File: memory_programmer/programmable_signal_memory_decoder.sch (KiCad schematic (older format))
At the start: 5 parts

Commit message: ram pcb
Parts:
- U3: renamed from U?; footprint (none) -> Package_DIP:DIP-16_W7.62mm_LongPads
- U4, U5, U6, U7: renamed from U?; footprint (none) -> Package_DIP:DIP-20_W7.62mm_LongPads
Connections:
- net D0: no longer U4.3 (D0), U5.3 (D0), U6.3 (D0)
- net D1: no longer U4.4 (D1), U5.4 (D1), U6.4 (D1), U7.4 (D1)
- net D2: no longer U4.7 (D2), U5.7 (D2), U6.7 (D2), U7.7 (D2)
- net D3: no longer U4.8 (D3), U5.8 (D3), U6.8 (D3), U7.8 (D3)
- net D4: no longer U4.13 (D4), U5.13 (D4), U6.13 (D4), U7.13 (D4)
- net D5: no longer U4.14 (D5), U5.14 (D5), U6.14 (D5), U7.14 (D5)
- net D6: no longer U4.17 (D6), U5.17 (D6), U6.17 (D6), U7.17 (D6)
- net D7: no longer U4.18 (D7), U5.18 (D7), U6.18 (D7), U7.18 (D7)
- net P0: now reaches U7.3 (D0)
- net P0: now also U4.3 (D0), U5.3 (D0), U6.3 (D0)
- net A0 renamed AD0
- net A1 renamed AD1
- net A10 renamed AD10
- net A11 renamed AD11
- net A12 renamed AD12
- net A13 renamed AD13
- net A14 renamed AD14
- net A15 renamed AD15
- net A2 renamed AD2
- net A3 renamed AD3
- net A4 renamed AD4
- net A5 renamed AD5
- net A6 renamed AD6
- net A7 renamed AD7
- net A8 renamed AD8
- net A9 renamed AD9
- new net P1: U4.4 (D1), U5.4 (D1), U6.4 (D1), U7.4 (D1)
- new net P2: U4.7 (D2), U5.7 (D2), U6.7 (D2), U7.7 (D2)
- new net P3: U4.8 (D3), U5.8 (D3), U6.8 (D3), U7.8 (D3)
- new net P4: U4.13 (D4), U5.13 (D4), U6.13 (D4), U7.13 (D4)
- new net P5: U4.14 (D5), U5.14 (D5), U6.14 (D5), U7.14 (D5)
- new net P6: U4.17 (D6), U5.17 (D6), U6.17 (D6), U7.17 (D6)
- new net P7: U4.18 (D7), U5.18 (D7), U6.18 (D7), U7.18 (D7)

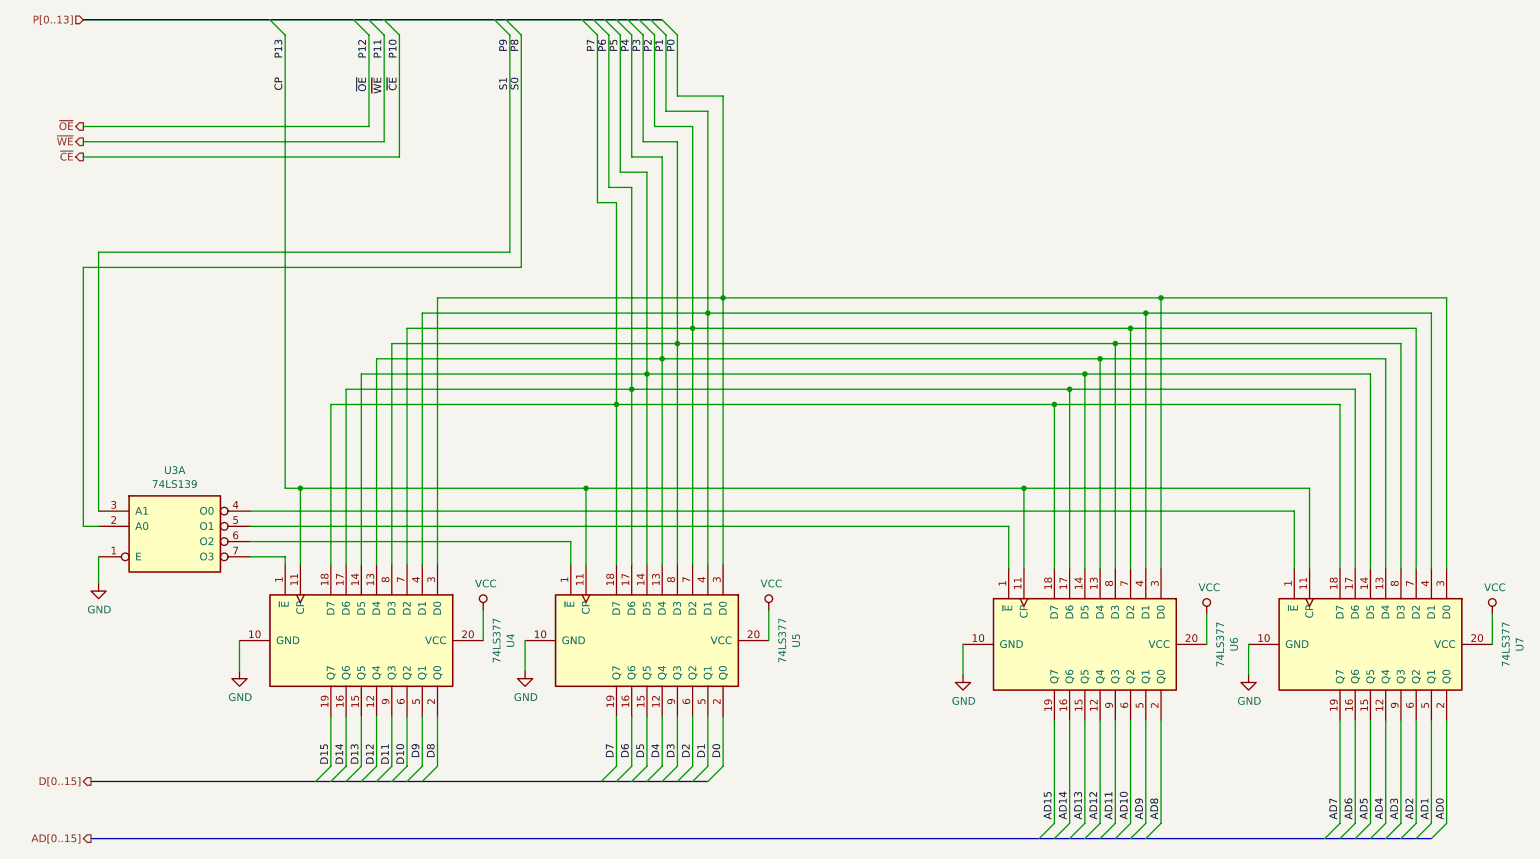
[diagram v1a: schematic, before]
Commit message: memory programmer and cu
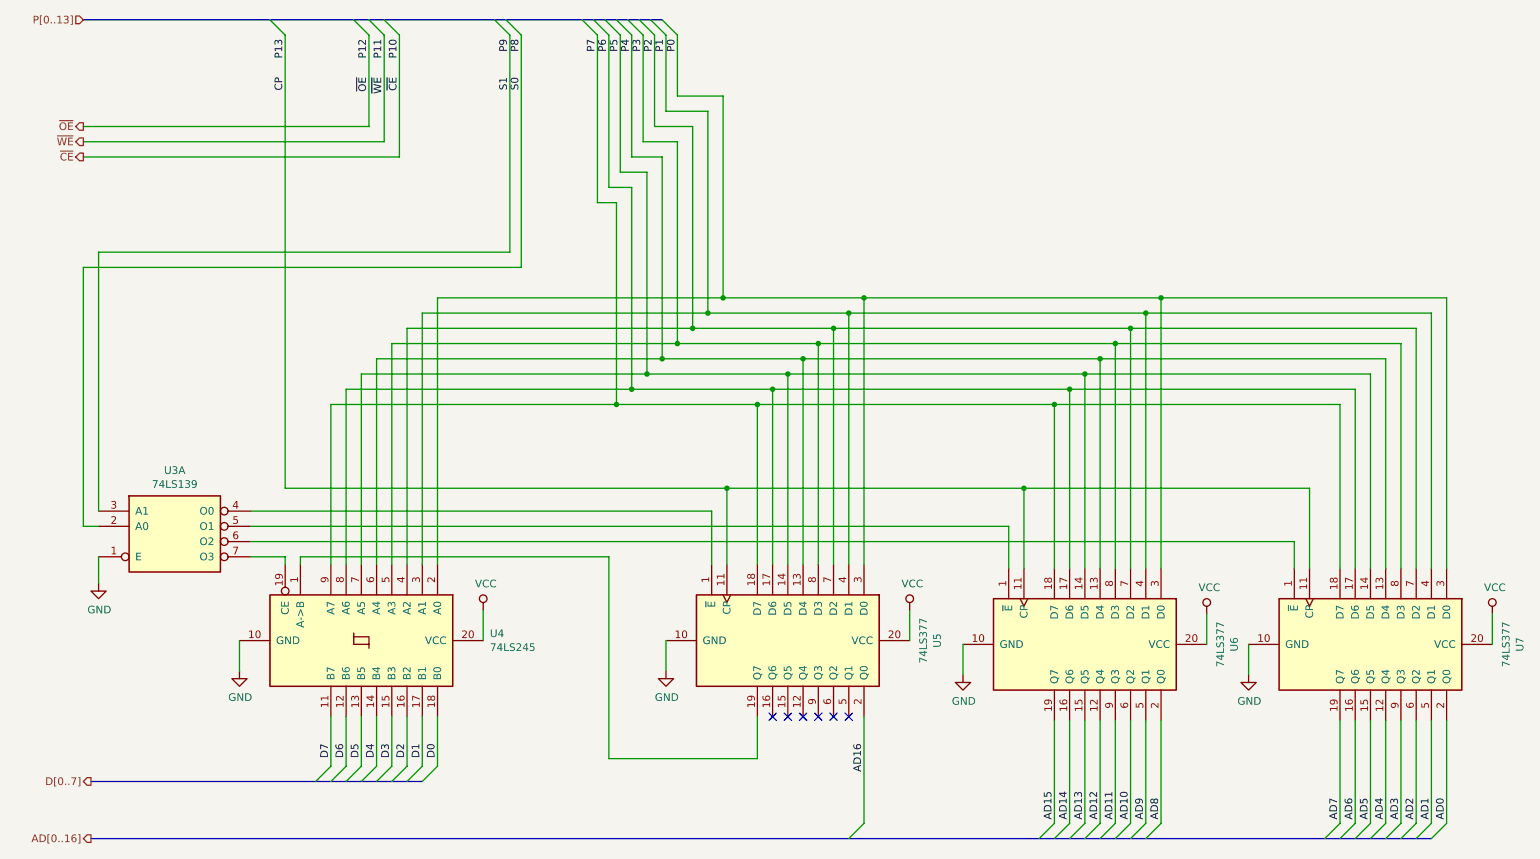
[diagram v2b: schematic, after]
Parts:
- removed U4: 74LS377, Package_DIP:DIP-20_W7.62mm_LongPads, symbol 74xx:74LS377
- added U4: 74LS245, Package_DIP:DIP-20_W7.62mm_LongPads, symbol 74xx:74LS245
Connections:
- net D0: now also U4.18 (B0); no longer U5.2 (Q0)
- net D1: now also U4.17 (B1); no longer U5.5 (Q1)
- net D2: now also U4.16 (B2); no longer U5.6 (Q2)
- net D3: now also U4.15 (B3); no longer U5.9 (Q3)
- net D4: now also U4.14 (B4); no longer U5.12 (Q4)
- net D5: now also U4.13 (B5); no longer U5.15 (Q5)
- net D6: now also U4.12 (B6); no longer U5.16 (Q6)
- net D7: now also U4.11 (B7); no longer U5.19 (Q7)
- net GND: now also U4.10 (GND)
- net P0: now also U4.2 (A0)
- net P1: now also U4.3 (A1)
- net P2: now also U4.4 (A2)
- net P3: now also U4.5 (A3)
- net P4: now also U4.6 (A4)
- net P5: now also U4.7 (A5)
- net P6: now also U4.8 (A6)
- net P7: now also U4.9 (A7)
- net VCC: now also U4.20 (VCC)
- net at U7.1 (~E): now also U3.6 (O2); no longer U3.4 (O0)
- net at U5.1 (~E): now also U3.4 (O0); no longer U3.6 (O2)
- net at U3.7 (O3): now also U4.19 (CE)
- new net: U4.1 (A->B), U5.19 (Q7)
- new net AD16: U5.2 (Q0)
- no-connect marks 0 -> 6
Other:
- moved on the sheet: U5
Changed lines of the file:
@@
 $Descr A4 11693 8268
 encoding utf-8
-Sheet 5 5
+Sheet 3 3
 Title ""
 Date ""
@@
 L 74xx:74LS377 U?
 U 1 1 5D3D9F68
-P 4725 5050
+P 5650 5050
 AR Path="/5D3716A7/5D3D9F68" Ref="U?"  Part="1"
 AR Path="/5D371796/5D3D9F68" Ref="U?"  Part="1"
@@
 AR Path="/5D35D52D/5D3B2113/5D3D9F68" Ref="U?"  Part="1"
 AR Path="/5EDF08FE/5D3D9F68" Ref="U5"  Part="1"
-F 0 "U5" H 4725 6031 50  0000 C CNN
-F 1 "74LS377" H 4725 5940 50  0000 C CNN
-F 2 "Package_DIP:DIP-20_W7.62mm_LongPads" H 4725 5050 50  0001 C CNN
-F 3 "http://www.ti.com/lit/gpn/sn74LS377" H 4725 5050 50  0001 C CNN
-	1    4725 5050
+F 0 "U5" H 5650 6031 50  0000 C CNN
+F 1 "74LS377" H 5650 5940 50  0000 C CNN
+F 2 "Package_DIP:DIP-20_W7.62mm_LongPads" H 5650 5050 50  0001 C CNN
+F 3 "http://www.ti.com/lit/gpn/sn74LS377" H 5650 5050 50  0001 C CNN
+	1    5650 5050
 	0    1    1    0
 $EndComp
@@
 L power:GND #PWR014
 U 1 1 5D3D9F6E
-P 3925 5250
-F 0 "#PWR014" H 3925 5000 50  0001 C CNN
-F 1 "GND" H 3930 5077 50  0000 C CNN
-F 2 "" H 3925 5250 50  0001 C CNN
-F 3 "" H 3925 5250 50  0001 C CNN
-	1    3925 5250
-	1    0    0    -1
-$EndComp
-Wire Wire Line
-	3925 5250 3925 5050
+P 4850 5250
+F 0 "#PWR014" H 4850 5000 50  0001 C CNN
+F 1 "GND" H 4855 5077 50  0000 C CNN
+F 2 "" H 4850 5250 50  0001 C CNN
+F 3 "" H 4850 5250 50  0001 C CNN
+	1    4850 5250
+	1    0    0    -1
+$EndComp
+Wire Wire Line
+	4850 5250 4850 5050
 $Comp
 L power:VCC #PWR015
 U 1 1 5D3D9F75
-P 5525 4850
-F 0 "#PWR015" H 5525 4700 50  0001 C CNN
-F 1 "VCC" H 5542 5023 50  0000 C CNN
-F 2 "" H 5525 4850 50  0001 C CNN
-F 3 "" H 5525 4850 50  0001 C CNN
-	1    5525 4850
-	1    0    0    -1
-$EndComp
-Wire Wire Line
-	5525 4850 5525 5050
-$Comp
-L 74xx:74LS377 U?
-U 1 1 5D3D9F7C
-P 2850 5050
-AR Path="/5D3716A7/5D3D9F7C" Ref="U?"  Part="1"
-AR Path="/5D371796/5D3D9F7C" Ref="U?"  Part="1"
-AR Path="/5D737E0E/5D3D9F7C" Ref="U?"  Part="1"
-AR Path="/5D35BA95/5D3D9F7C" Ref="U?"  Part="1"
-AR Path="/5D35CB6B/5D3D9F7C" Ref="U?"  Part="1"
-AR Path="/5D35D52D/5D3B2113/5D3D9F7C" Ref="U?"  Part="1"
-AR Path="/5EDF08FE/5D3D9F7C" Ref="U4"  Part="1"
-F 0 "U4" H 2850 6031 50  0000 C CNN
-F 1 "74LS377" H 2850 5940 50  0000 C CNN
-F 2 "Package_DIP:DIP-20_W7.62mm_LongPads" H 2850 5050 50  0001 C CNN
-F 3 "http://www.ti.com/lit/gpn/sn74LS377" H 2850 5050 50  0001 C CNN
-	1    2850 5050
-	0    1    1    0
-$EndComp
+P 6450 4850
+F 0 "#PWR015" H 6450 4700 50  0001 C CNN
+F 1 "VCC" H 6467 5023 50  0000 C CNN
+F 2 "" H 6450 4850 50  0001 C CNN
+F 3 "" H 6450 4850 50  0001 C CNN
+	1    6450 4850
+	1    0    0    -1
+$EndComp
+Wire Wire Line
+	6450 4850 6450 5050
 $Comp
 L power:GND #PWR012
@@
 	2350 4500 2350 4550
 Wire Wire Line
-	4225 4400 4225 4550
-Wire Wire Line
 	2125 4300 7100 4300
 Wire Wire Line
 	7100 4300 7100 4575
-Wire Wire Line
-	8975 4200 8975 4575
 Wire Wire Line
 	1125 2500 3825 2500
@@
 	1125 4675 1125 4500
 Wire Wire Line
-	2450 4050 2350 4050
-Wire Wire Line
 	2350 1075 2350 4050
-Wire Wire Line
-	2450 4050 2450 4550
-Connection ~ 2450 4050
 Wire Wire Line
 	7200 4050 7200 4575
@@
 Wire Wire Line
 	7200 4050 9075 4050
-Wire Wire Line
-	2125 4400 4225 4400
 Connection ~ 4525 3500
 Wire Wire Line
-	4525 4550 4525 3500
+	5450 4550 5450 3500
 Connection ~ 4725 3300
 Wire Wire Line
@@
 Connection ~ 4625 3400
 Wire Wire Line
-	4625 3400 4625 4550
+	5550 3400 5550 4550
 Connection ~ 4825 3200
 Connection ~ 4925 3100
@@
 Connection ~ 5225 2800
 Wire Wire Line
-	4725 3300 4725 4550
-Wire Wire Line
-	4825 3200 4825 4550
-Wire Wire Line
-	4925 3100 4925 4550
+	5650 3300 5650 4550
+Wire Wire Line
+	5750 3200 5750 4550
+Wire Wire Line
+	5850 3100 5850 4550
 Wire Wire Line
 	9575 3200 9575 4575
@@
 	9875 2900 9875 4575
 Text HLabel 1075 6350 0    50   Output ~ 0
-AD[0..15]
+AD[0..16]
 Entry Wire Line
 	7300 6350 7400 6250
@@
 Wire Wire Line
 	7800 5575 7800 6250
-Entry Wire Line
-	5225 5875 5125 5975
-Text Label 5225 5725 3    50   ~ 0
-D0
-Entry Wire Line
-	5125 5875 5025 5975
-Text Label 5125 5725 3    50   ~ 0
-D1
-Entry Wire Line
-	5025 5875 4925 5975
-Text Label 5025 5725 3    50   ~ 0
-D2
-Entry Wire Line
-	4925 5875 4825 5975
-Text Label 4925 5725 3    50   ~ 0
-D3
-Entry Wire Line
-	4825 5875 4725 5975
-Text Label 4825 5725 3    50   ~ 0
-D4
-Entry Wire Line
-	4725 5875 4625 5975
-Text Label 4725 5725 3    50   ~ 0
-D5
-Entry Wire Line
-	4625 5875 4525 5975
-Text Label 4625 5725 3    50   ~ 0
-D6
-Entry Wire Line
-	4525 5875 4425 5975
-Text Label 4525 5725 3    50   ~ 0
-D7
-Entry Wire Line
-	3350 5875 3250 5975
-Text Label 3350 5725 3    50   ~ 0
-D8
-Entry Wire Line
-	3250 5875 3150 5975
-Text Label 3250 5725 3    50   ~ 0
-D9
-Entry Wire Line
-	3150 5875 3050 5975
-Text Label 3150 5725 3    50   ~ 0
-D10
-Entry Wire Line
-	3050 5875 2950 5975
-Text Label 3050 5725 3    50   ~ 0
-D11
-Entry Wire Line
-	2950 5875 2850 5975
-Text Label 2950 5725 3    50   ~ 0
-D12
-Entry Wire Line
-	2850 5875 2750 5975
-Text Label 2850 5725 3    50   ~ 0
-D13
-Entry Wire Line
-	2750 5875 2650 5975
-Text Label 2750 5725 3    50   ~ 0
-D14
-Entry Wire Line
-	2650 5875 2550 5975
-Text Label 2650 5725 3    50   ~ 0
-D15
+Text Label 6150 5725 3    50   ~ 0
+AD16
 Text HLabel 1075 5975 0    50   Output ~ 0
-D[0..15]
-Wire Wire Line
-	5225 5550 5225 5875
-Wire Wire Line
-	5125 5550 5125 5875
-Wire Wire Line
-	5025 5550 5025 5875
-Wire Wire Line
-	4925 5550 4925 5875
-Wire Wire Line
-	4825 5550 4825 5875
-Wire Wire Line
-	4725 5550 4725 5875
-Wire Wire Line
-	4625 5550 4625 5875
-Wire Wire Line
-	4525 5550 4525 5875
-Wire Wire Line
-	3350 5550 3350 5875
-Wire Wire Line
-	3250 5550 3250 5875
-Wire Wire Line
-	3150 5550 3150 5875
-Wire Wire Line
-	3050 5550 3050 5875
-Wire Wire Line
-	2950 5550 2950 5875
-Wire Wire Line
-	2850 5550 2850 5875
-Wire Wire Line
-	2750 5550 2750 5875
-Wire Wire Line
-	2650 5550 2650 5875
+D[0..7]
 Wire Wire Line
 	2900 1075 2900 1675
@@
 ~CE~
 Wire Wire Line
-	2125 4200 8975 4200
-Wire Wire Line
-	4325 4550 4325 4050
-Wire Wire Line
-	2450 4050 4325 4050
-Connection ~ 4325 4050
-Wire Wire Line
-	4325 4050 7200 4050
-Wire Wire Line
-	5025 3000 5025 4550
-Wire Wire Line
-	5125 2900 5125 4550
-Wire Wire Line
-	5225 2800 5225 4550
+	2125 4200 5150 4200
+Wire Wire Line
+	5250 4550 5250 4050
+Wire Wire Line
+	5950 3000 5950 4550
+Wire Wire Line
+	6050 2900 6050 4550
+Wire Wire Line
+	6150 2800 6150 4550
 Wire Wire Line
 	2650 4550 2650 3500
@@
 	9975 4575 9975 2800
 Wire Wire Line
-	5125 2900 8000 2900
-Wire Wire Line
-	5225 2800 8100 2800
-Wire Wire Line
-	5025 3000 7900 3000
-Wire Wire Line
-	4825 3200 7700 3200
-Wire Wire Line
-	4925 3100 7800 3100
-Wire Wire Line
-	4725 3300 7600 3300
-Wire Wire Line
-	4625 3400 7500 3400
-Wire Wire Line
-	4525 3500 7400 3500
+	5125 2900 6050 2900
+Wire Wire Line
+	5225 2800 6150 2800
+Wire Wire Line
+	5025 3000 5950 3000
+Wire Wire Line
+	4825 3200 5750 3200
+Wire Wire Line
+	4925 3100 5850 3100
+Wire Wire Line
+	4725 3300 5650 3300
+Wire Wire Line
+	4625 3400 5550 3400
+Wire Wire Line
+	4525 3500 5450 3500
 Wire Wire Line
 	7700 3200 7700 4575
@@
 Text HLabel 1025 975  0    50   Input ~ 0
 P[0..13]
+Entry Wire Line
+	3350 5875 3250 5975
+Text Label 3350 5725 3    50   ~ 0
+D0
+Entry Wire Line
+	3250 5875 3150 5975
+Text Label 3250 5725 3    50   ~ 0
+D1
+Entry Wire Line
+	3150 5875 3050 5975
+Text Label 3150 5725 3    50   ~ 0
+D2
+Entry Wire Line
+	3050 5875 2950 5975
+Text Label 3050 5725 3    50   ~ 0
+D3
+Entry Wire Line
+	2950 5875 2850 5975
+Text Label 2950 5725 3    50   ~ 0
+D4
+Entry Wire Line
+	2850 5875 2750 5975
+Text Label 2850 5725 3    50   ~ 0
+D5
+Entry Wire Line
+	2750 5875 2650 5975
+Text Label 2750 5725 3    50   ~ 0
+D6
+Entry Wire Line
+	2650 5875 2550 5975
+Text Label 2650 5725 3    50   ~ 0
+D7
+Wire Wire Line
+	3350 5550 3350 5875
+Wire Wire Line
+	3250 5550 3250 5875
+Wire Wire Line
+	3150 5550 3150 5875
+Wire Wire Line
+	3050 5550 3050 5875
+Wire Wire Line
+	2950 5550 2950 5875
+Wire Wire Line
+	2850 5550 2850 5875
+Wire Wire Line
+	2750 5550 2750 5875
+Wire Wire Line
+	2650 5550 2650 5875
+Connection ~ 5250 4050
+Wire Wire Line
+	5250 4050 7200 4050
+Connection ~ 5450 3500
+Wire Wire Line
+	5450 3500 7400 3500
+Connection ~ 5550 3400
+Wire Wire Line
+	5550 3400 7500 3400
+Connection ~ 5650 3300
+Wire Wire Line
+	5650 3300 7600 3300
+Connection ~ 5750 3200
+Wire Wire Line
+	5750 3200 7700 3200
+Connection ~ 5850 3100
+Wire Wire Line
+	5850 3100 7800 3100
+Connection ~ 5950 3000
+Wire Wire Line
+	5950 3000 7900 3000
+Connection ~ 6050 2900
+Wire Wire Line
+	6050 2900 8000 2900
+Connection ~ 6150 2800
+Wire Wire Line
+	6150 2800 8100 2800
+Entry Wire Line
+	6050 6350 6150 6250
+Wire Wire Line
+	6150 5550 6150 6250
+NoConn ~ 5550 5550
+NoConn ~ 5650 5550
+NoConn ~ 5750 5550
+NoConn ~ 5850 5550
+NoConn ~ 5950 5550
+NoConn ~ 6050 5550
+Wire Wire Line
+	2350 4050 5250 4050
+$Comp
+L 74xx:74LS245 U4
+U 1 1 5F53CE48
+P 2850 5050
+F 0 "U4" V 2804 5894 50  0000 L CNN
+F 1 "74LS245" V 2895 5894 50  0000 L CNN
+F 2 "Package_DIP:DIP-20_W7.62mm_LongPads" H 2850 5050 50  0001 C CNN
+F 3 "http://www.ti.com/lit/gpn/sn74LS245" H 2850 5050 50  0001 C CNN
+	1    2850 5050
+	0    1    1    0
+$EndComp
+Wire Wire Line
+	2450 4550 2450 4500
+Wire Wire Line
+	2450 4500 4475 4500
+Wire Wire Line
+	4475 4500 4475 5825
+Wire Wire Line
+	4475 5825 5450 5825
+Wire Wire Line
+	5450 5825 5450 5550
+Wire Wire Line
+	5150 4200 5150 4400
+Wire Bus Line
+	1075 5975 3250 5975
 Wire Bus Line
 	1025 975  4825 975
 Wire Bus Line
-	1075 5975 5125 5975
-Wire Bus Line
 	1075 6350 9875 6350
+Wire Wire Line
+	5150 4400 5150 4550
+Wire Wire Line
+	8975 4400 8975 4575
+Wire Wire Line
+	2125 4400 8975 4400
 $EndSCHEMATC
